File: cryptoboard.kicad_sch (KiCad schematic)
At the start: 27 parts, among them J1 USB_A, J2 BOOT, J3 SWD, SW1 SW_Push, U1 STM32F103C8Tx, U2 LM317_SOT-223-3.3V

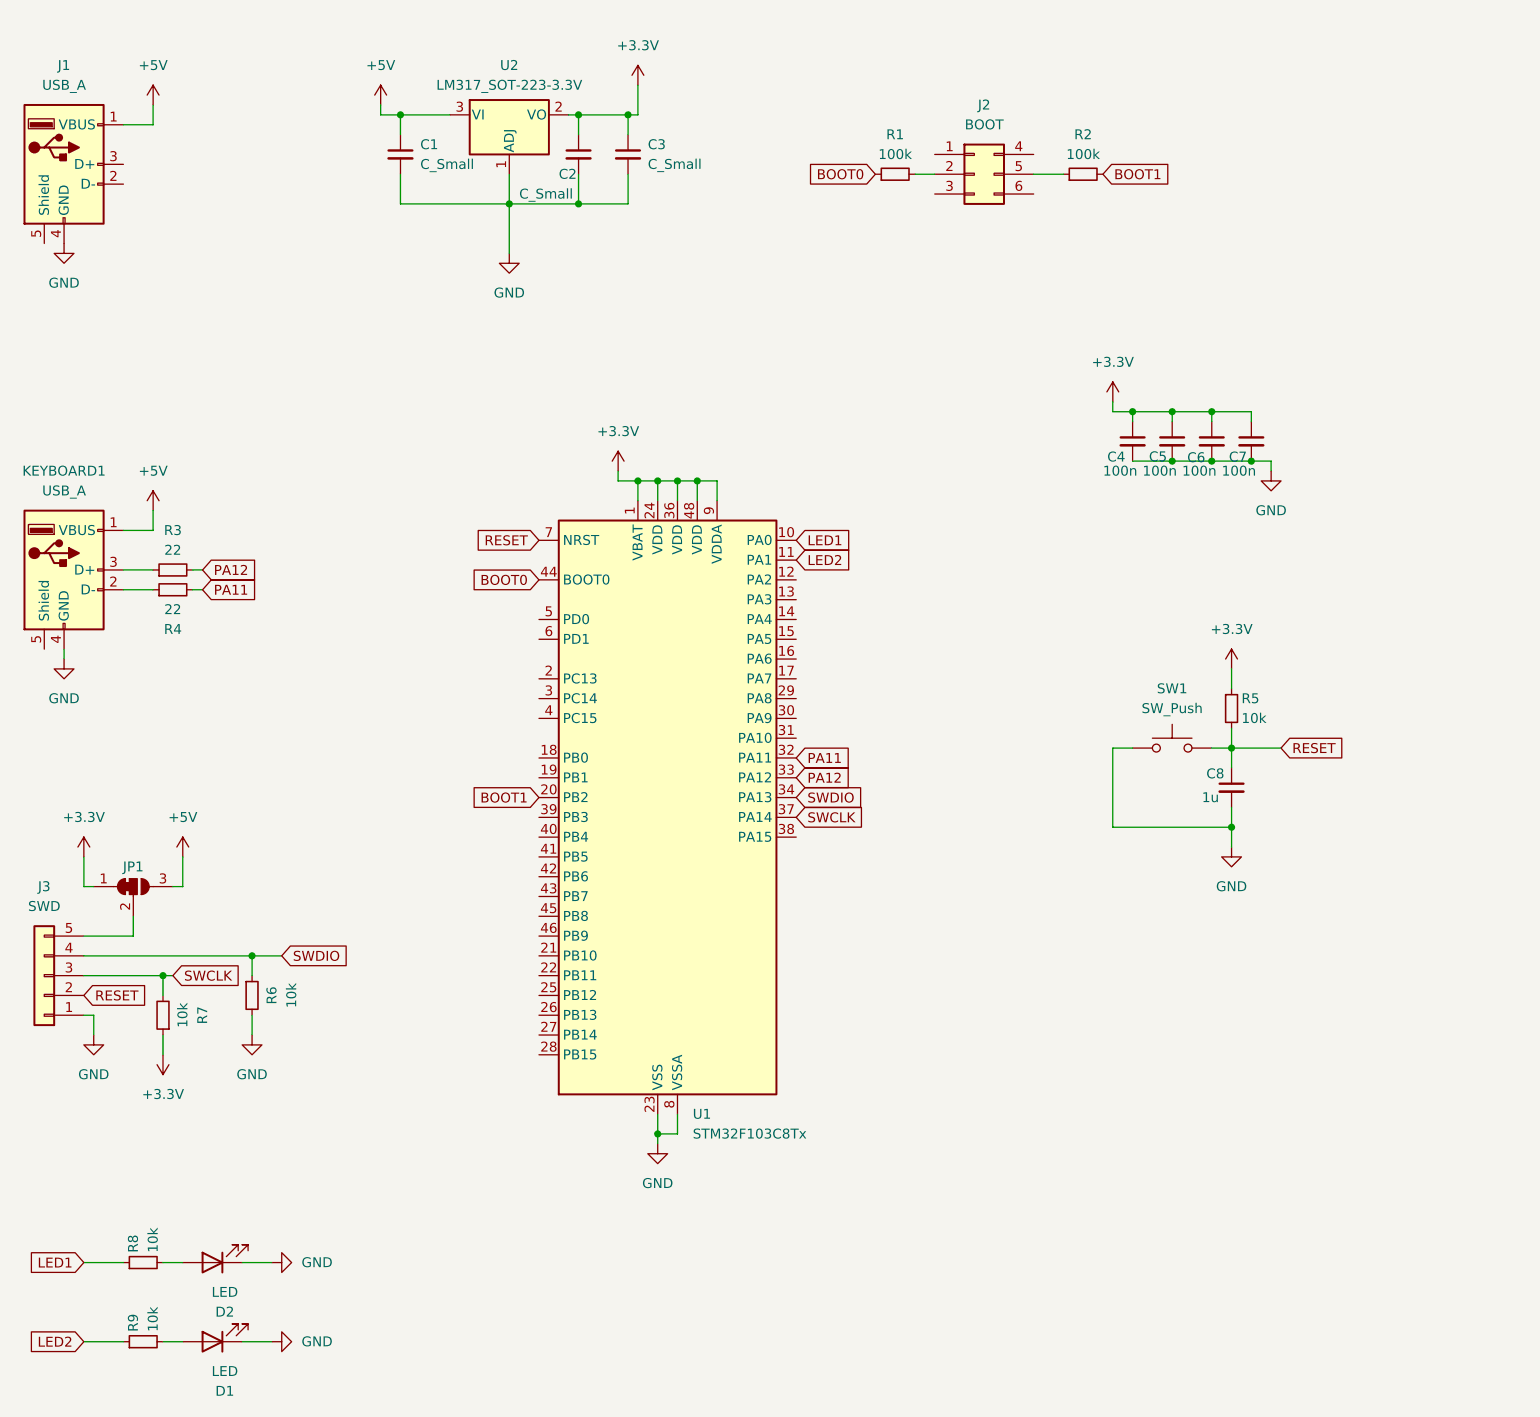
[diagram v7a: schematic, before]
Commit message: add usr es1
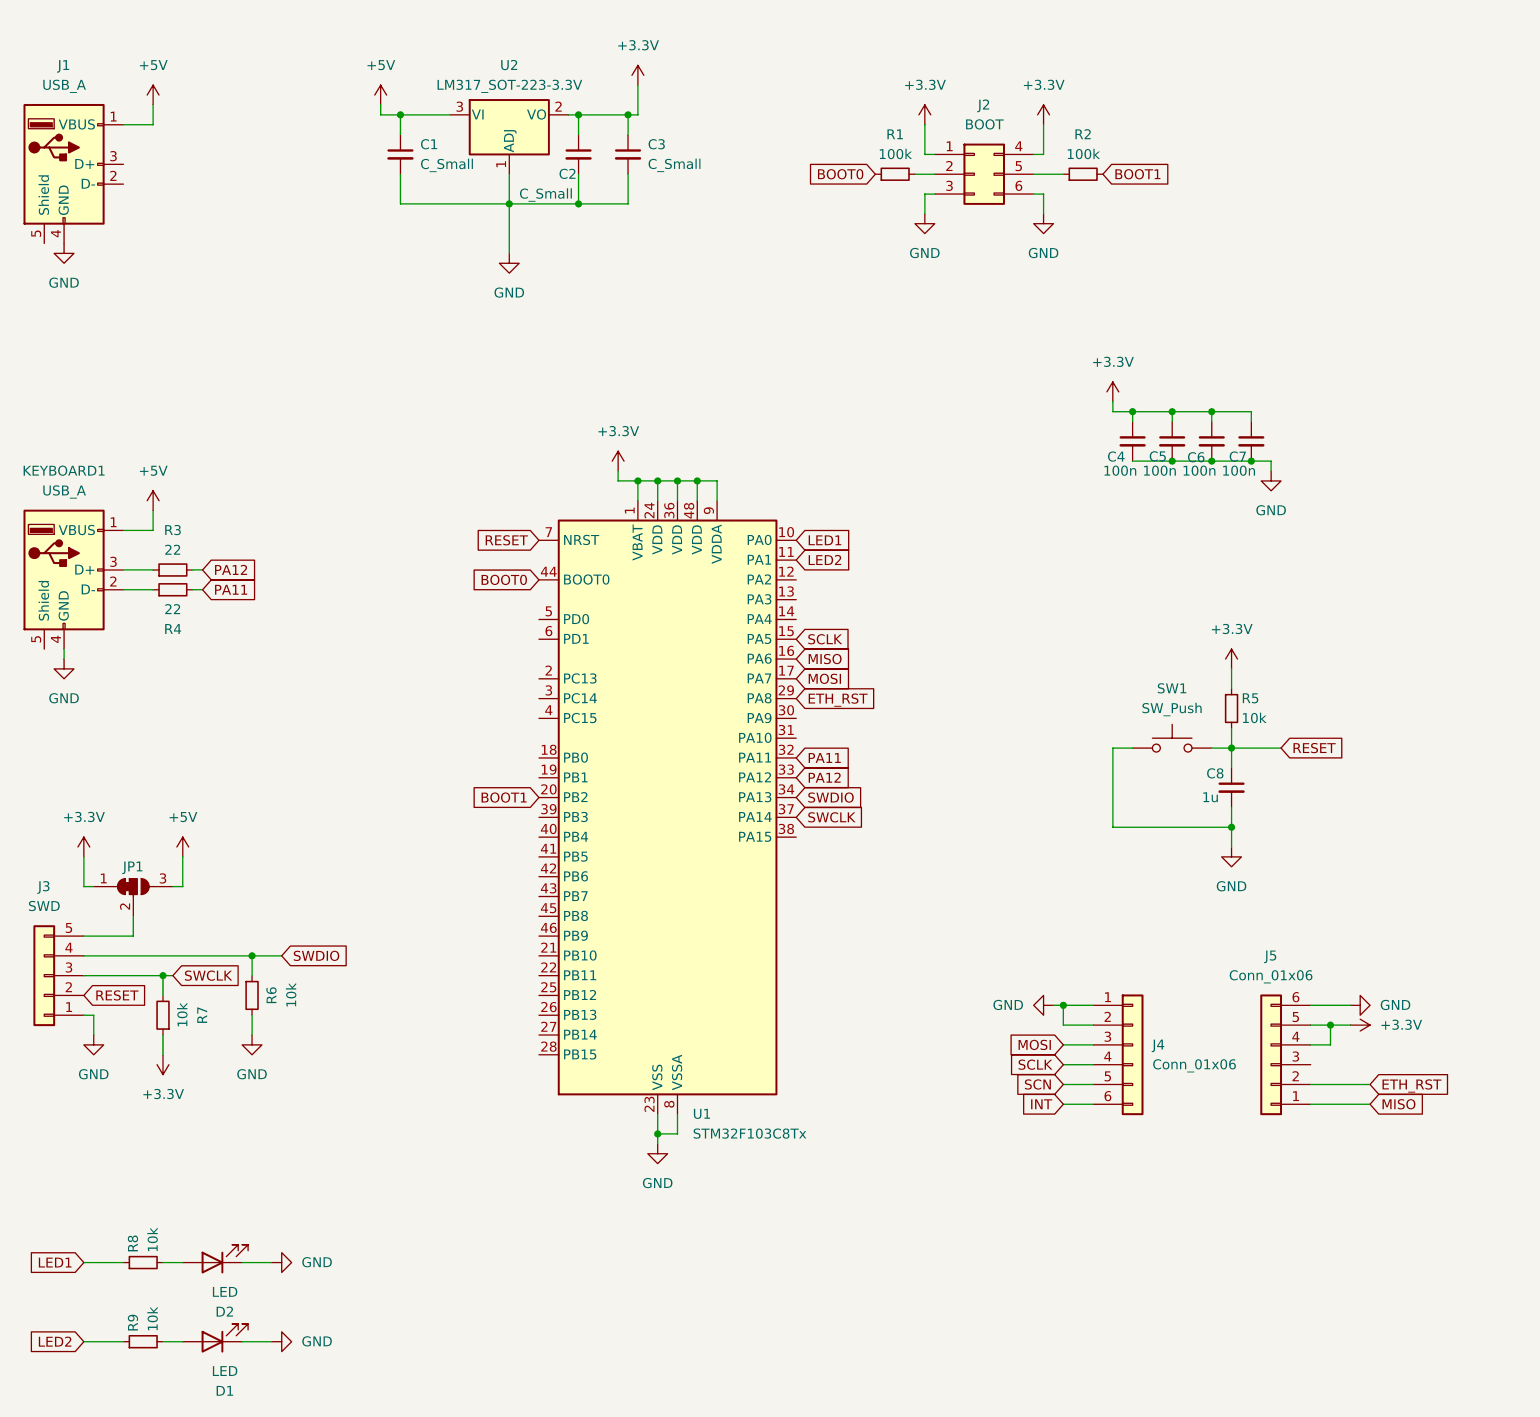
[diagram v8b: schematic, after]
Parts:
- added J4, J5: Conn_01x06, symbol Connector_Generic:Conn_01x06
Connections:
- net +3.3V: now also J2.1 (Pin_1), J2.4 (Pin_4), J5.4 (Pin_4), J5.5 (Pin_5)
- net GND: now also J2.3 (Pin_3), J2.6 (Pin_6), J4.1 (Pin_1), J4.2 (Pin_2), J5.6 (Pin_6)
- net SCLK: now reaches U1.15 (PA5)
- net SCLK: now also J4.4 (Pin_4)
- net MISO: now reaches U1.16 (PA6)
- net MISO: now also J5.1 (Pin_1)
- net MOSI: now reaches U1.17 (PA7)
- net MOSI: now also J4.3 (Pin_3)
- net ETH_RST: now reaches U1.29 (PA8)
- net ETH_RST: now also J5.2 (Pin_2)
- new net INT: J4.6 (Pin_6)
- new net SCN: J4.5 (Pin_5)
